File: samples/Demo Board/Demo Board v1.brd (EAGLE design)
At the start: 88.9 x 50.8 mm, 56 parts

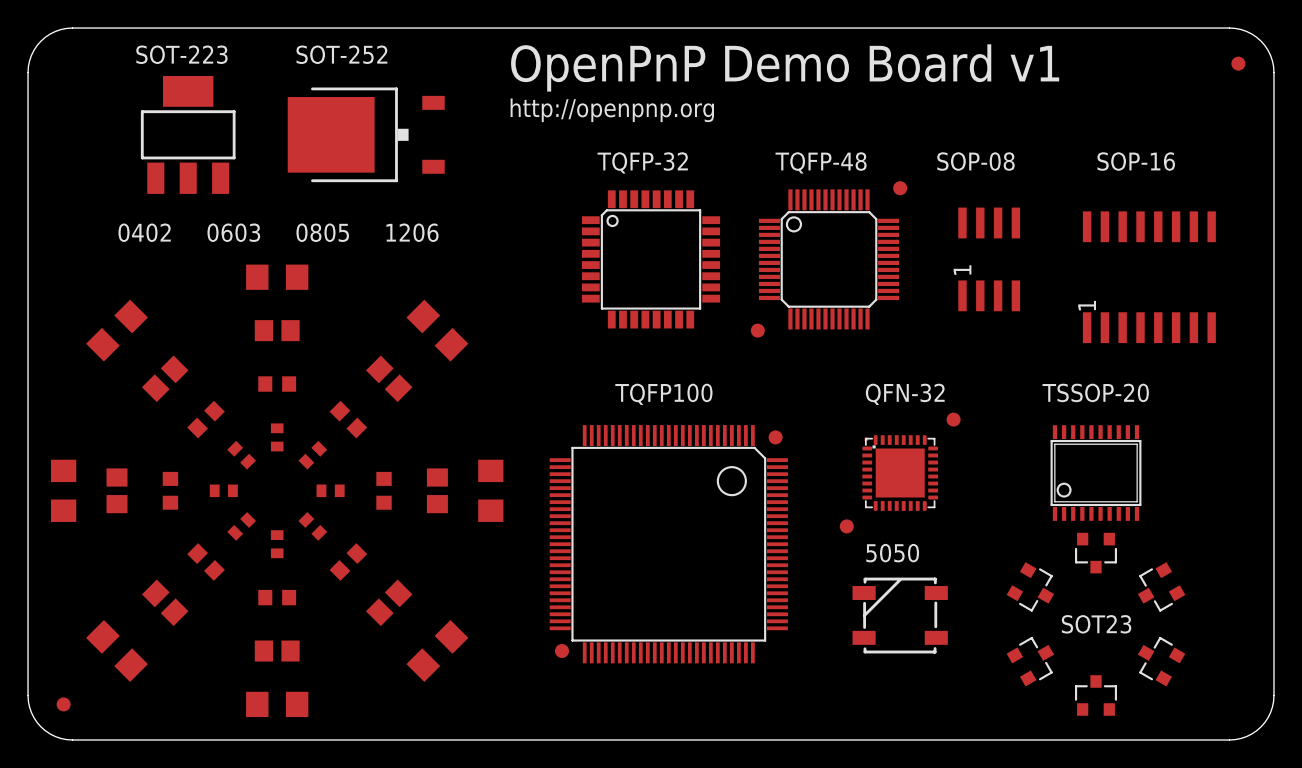
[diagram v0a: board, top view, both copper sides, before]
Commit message: Errata updates to the demo boards.
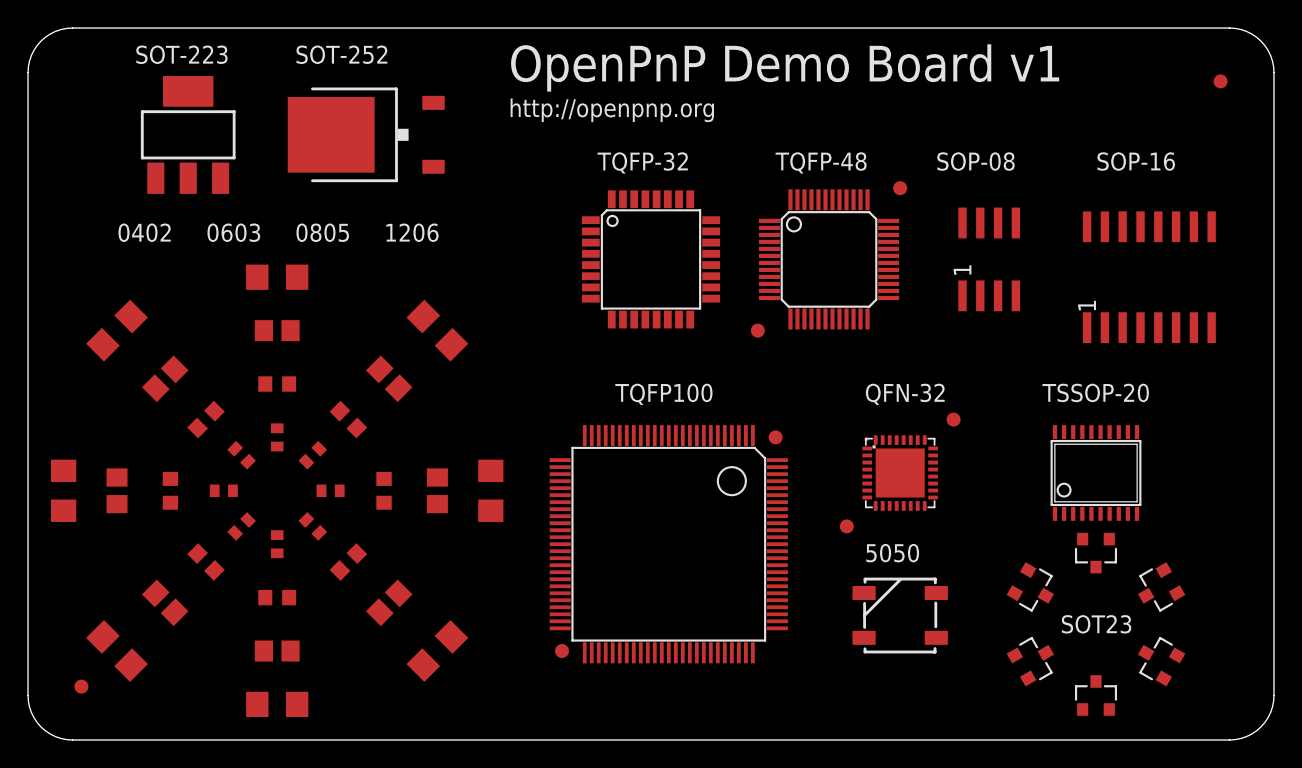
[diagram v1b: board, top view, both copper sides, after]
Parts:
- moved E$22 1.80 mm to (3.81, 3.81)
- moved E$13 1.80 mm to (85.1, 47.0)
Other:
- board text added: "* FIDS are missing keepout"
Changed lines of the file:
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@@
 <wire x1="85.725" y1="50.8" x2="3.175" y2="50.8" width="0" layer="20"/>
 <wire x1="3.175" y1="50.8" x2="0" y2="47.625" width="0" layer="20" curve="90"/>
+<text x="1.27" y="63.5" size="1.778" layer="48">* FIDS are missing keepout</text>
 </plain>
 <attributes>
@@
 <attribute name="VALUE" x="50.8" y="37.211" size="1.27" layer="27" ratio="10" rot="R270"/>
 </element>
-<element name="E$22" library="SparkFun-Aesthetics" package="FIDUCIAL-1X2" value="" x="2.54" y="2.54"/>
-<element name="E$13" library="SparkFun-Aesthetics" package="FIDUCIAL-1X2" value="" x="86.36" y="48.26"/>
+<element name="E$22" library="SparkFun-Aesthetics" package="FIDUCIAL-1X2" value="" x="3.81" y="3.81"/>
+<element name="E$13" library="SparkFun-Aesthetics" package="FIDUCIAL-1X2" value="" x="85.09" y="46.99"/>
 <element name="E$14" library="SparkFun-Aesthetics" package="FIDUCIAL-1X2" value="" x="38.1" y="6.35"/>
 <element name="E$15" library="SparkFun-Aesthetics" package="FIDUCIAL-1X2" value="" x="53.34" y="21.59"/>

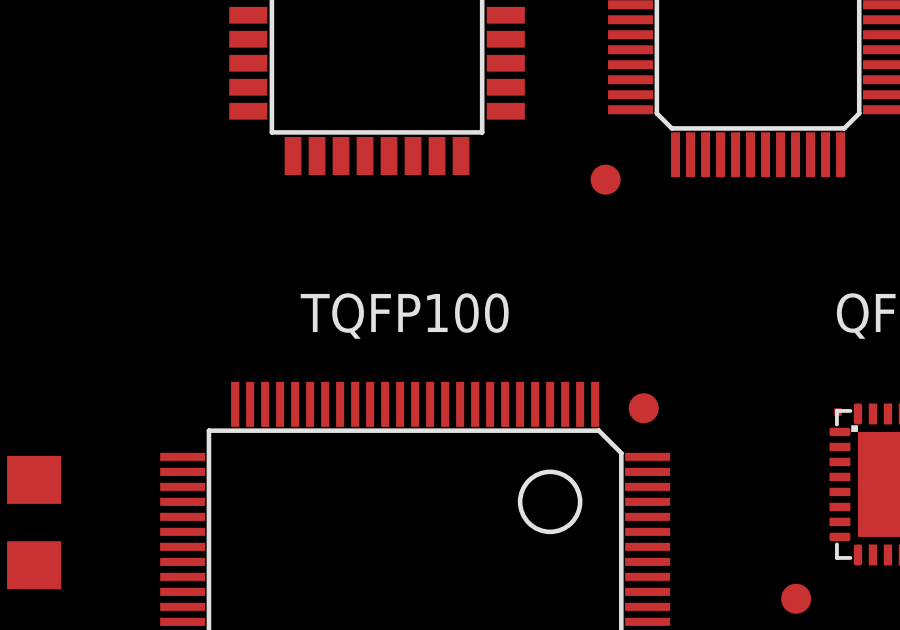
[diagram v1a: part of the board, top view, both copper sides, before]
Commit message: Renamed all the parts in the demo board to have useful names.
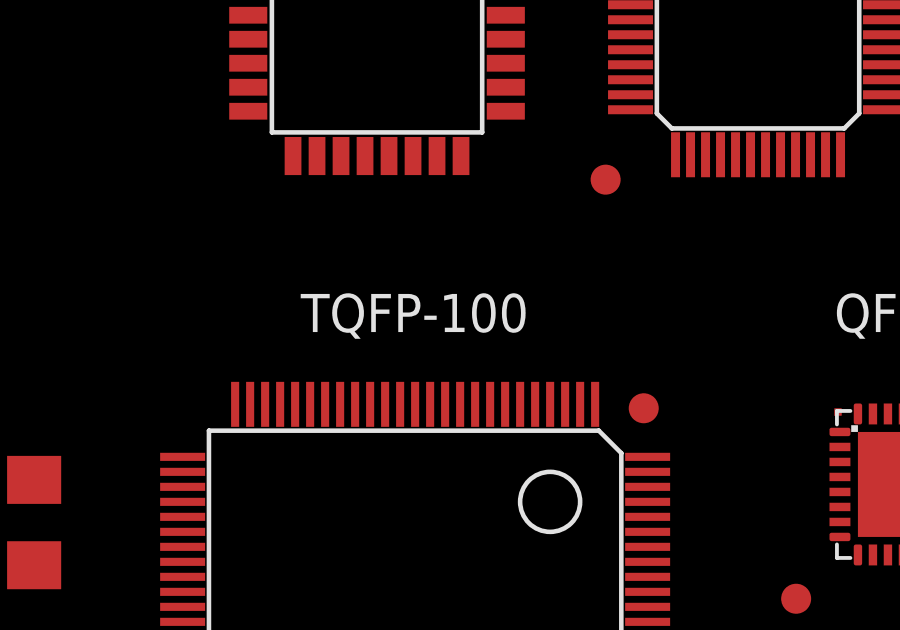
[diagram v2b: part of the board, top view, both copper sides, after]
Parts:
- renumbered E$1 to 5050, E$10 to TSSOP-20, E$11 to TQFP-32, E$12 to TQFP-48, E$13 to FID-2, E$14 to FID-5, E$15 to FID-6, E$16 to TQFP-100, E$17 to FID-3, E$18 to FID-4, E$19 to FID-7, E$2 to R1206-3, E$20 to FID-8, E$22 to FID-1, E$23 to R0402-1, E$24 to R0402-3, E$25 to R0402-5, E$26 to R0402-7, E$27 to R0402-2, E$28 to R0402-6, E$29 to R0402-8, E$3 to R1206-5, E$30 to R0402-4, E$31 to R0603-1, E$34 to R0603-5, E$35 to R0603-3, E$36 to R0603-7, E$37 to R0603-2, E$38 to R0603-4, E$39 to R0603-6, E$4 to SOP-16, E$40 to R0603-8, E$41 to R0805-1, E$42 to QFN-32, E$44 to R0805-3, E$45 to R0805-5, E$46 to R0805-7, E$47 to R0805-8, E$48 to R0805-6, E$5 to R1206-7, E$51 to SOT-223, E$52 to SOT-252, E$53 to SOP-08, E$54 to R0805-4, E$55 to R0805-2, E$56 to SOT-23-5, E$57 to SOT-23-6, E$58 to SOT-23-2, E$6 to R1206-8, E$60 to SOT-23-1, E$61 to SOT-23-4, E$62 to SOT-23-3, E$7 to R1206-2, E$8 to R1206-4, E$82 to R1206-1, E$9 to R1206-6
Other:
- board text added: "TQFP-100"
- board text removed: "TQFP100"
